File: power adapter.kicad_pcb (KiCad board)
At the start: 2 copper layers, 63.5 x 38.1 mm, 12 parts

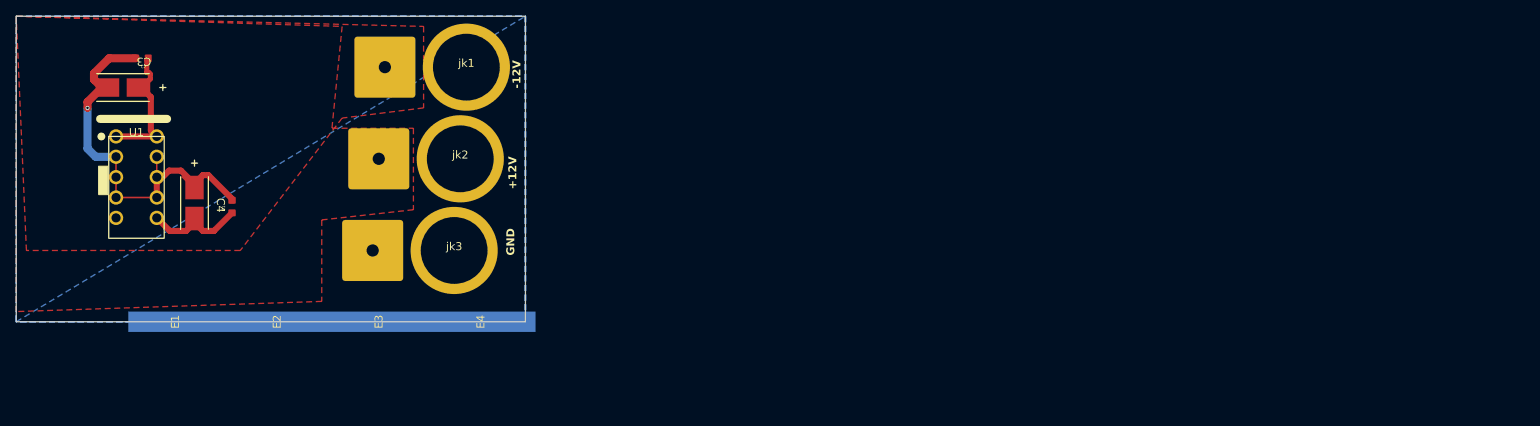
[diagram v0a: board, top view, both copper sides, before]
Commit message: added new board outline
used an .svg file from corel to define board outlinr and resized the banana jack holes and scale for the model
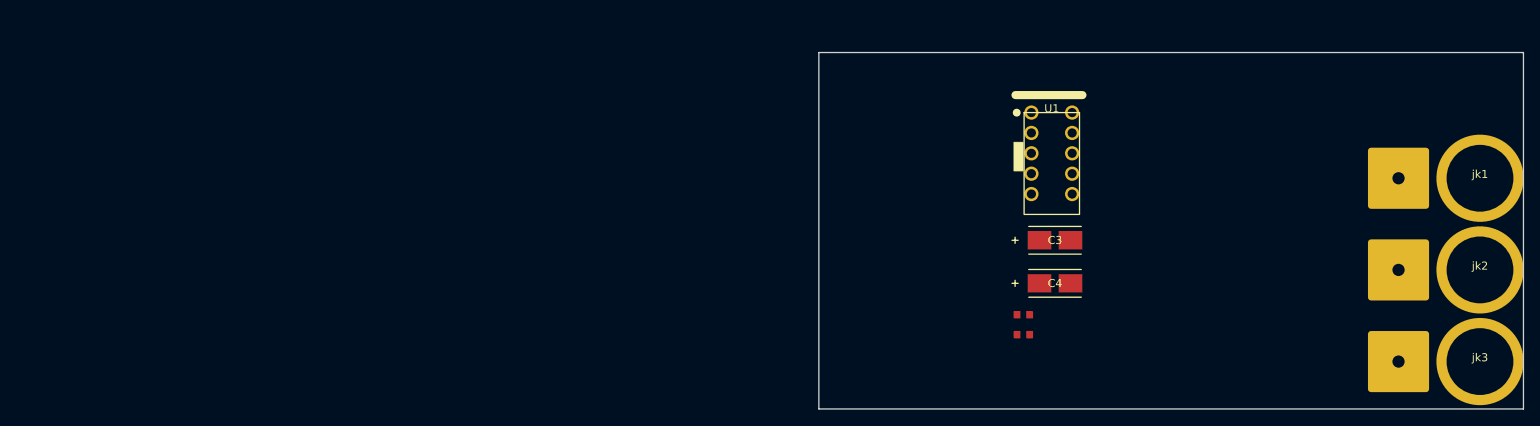
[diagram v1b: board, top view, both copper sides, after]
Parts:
- removed E1, E2, E3, E4: ~, adpterpcblib:edge
- moved jk3 128.7 mm to (207.9, 119.3)
- moved jk2 127.9 mm to (207.9, 107.8)
- moved jk1 127.2 mm to (207.9, 96.4)
- moved C3 117.8 mm to (154.9, 104.1), turned to 0 degrees
- moved C2 115.2 mm to (151.0, 115.9), turned to 0 degrees
- moved U1 114.2 mm to (154.5, 88.2)
- moved C4 107.8 mm to (154.9, 109.5), turned to 0 degrees
- moved C1 99.6 mm to (151.0, 113.4), turned to 0 degrees
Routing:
- net GND: track 55.3 -> 0.00 mm, vias 1 -> 0
- net +12V: track 17.0 -> 0.00 mm
- net -12V: track 12.4 -> 0.00 mm
- removed copper zone on B.Cu, net (none)
- removed copper zone on B.Cu, net +12V
- removed copper zone on F.Cu, net +12V
- removed copper zone on F.Cu, net -12V
- removed copper zone on B.Cu, net GND
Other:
- board size 63.5 x 38.1 mm -> 87.9 x 44.5 mm
- board text removed: "+12V"
- board text removed: "-12V"
- board text removed: "GND"

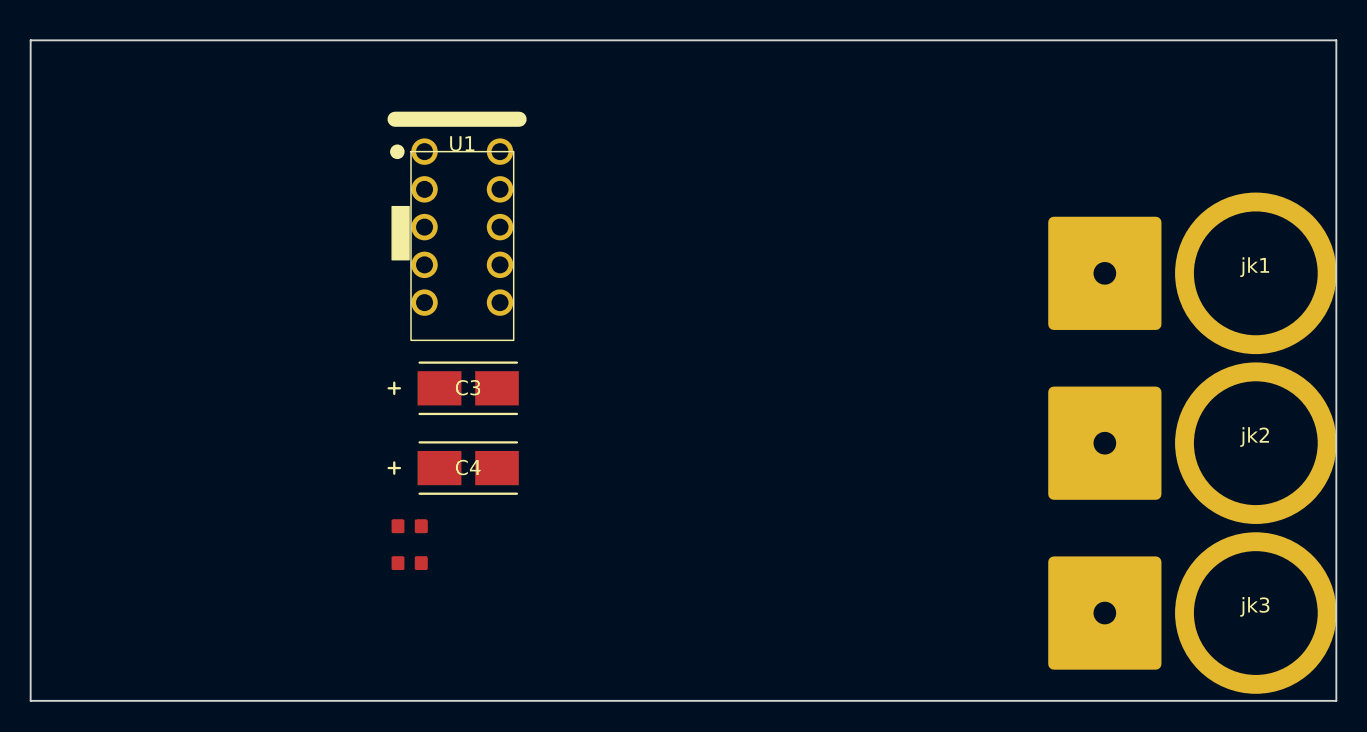
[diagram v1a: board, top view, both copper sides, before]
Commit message: added dimensions
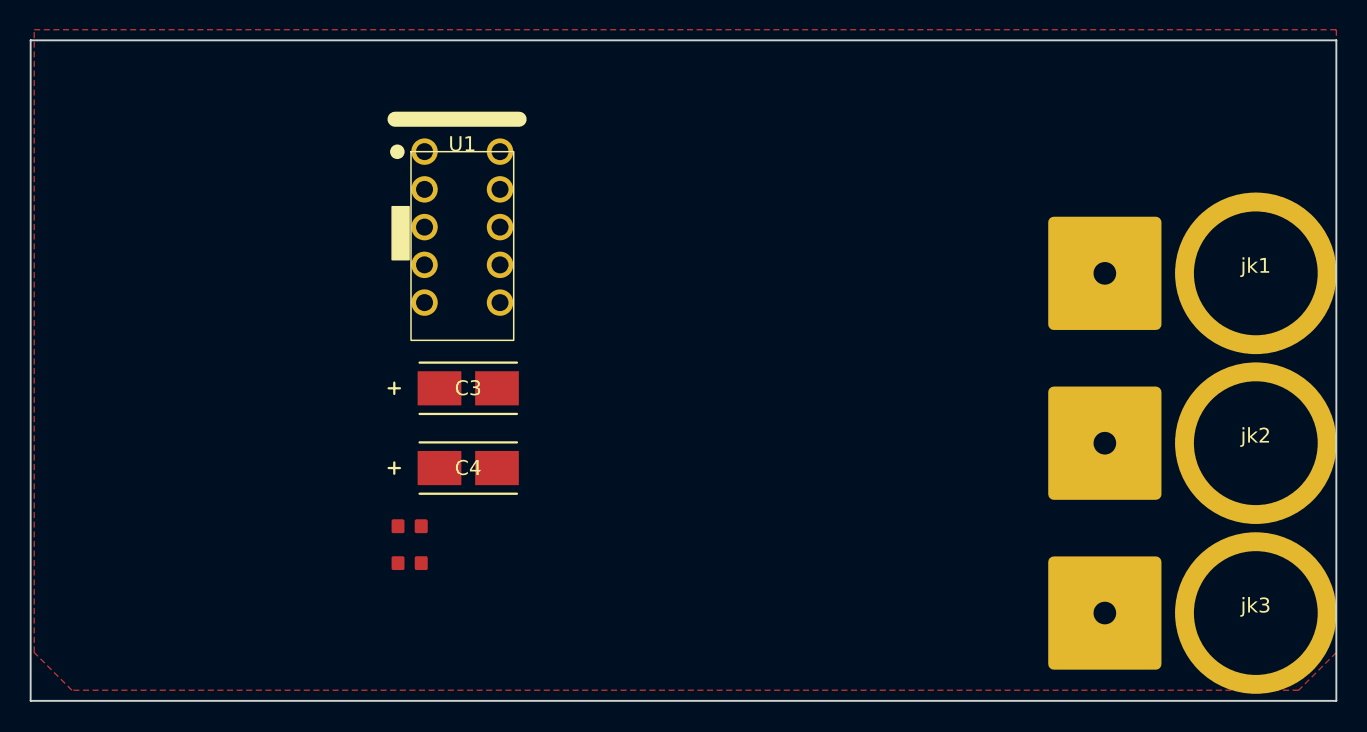
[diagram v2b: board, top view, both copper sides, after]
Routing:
- added copper zone on F.Cu, net GND
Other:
- board text added: "+12V"
- board text added: "-12V"
- board text added: "GND"
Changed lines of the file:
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@@
 		(layer "Edge.Cuts")
+	)
+	(gr_text "-12V"
+		(at 186.85 98.38 0)
+		(layer "F.Mask" knockout)
+		(effects
+			(font
+				(size 1 1)
+				(thickness 0.2)
+				(bold yes)
+			)
+			(justify left bottom)
+		)
+	)
+	(gr_text "GND"
+		(at 187.29 119 0)
+		(layer "F.Mask" knockout)
+		(effects
+			(font
+				(size 1 1)
+				(thickness 0.2)
+				(bold yes)
+			)
+			(justify left bottom)
+		)
+	)
+	(gr_text "+12V"
+		(at 185.36 109.38 0)
+		(layer "F.Mask" knockout)
+		(effects
+			(font
+				(size 1 1)
+				(thickness 0.2)
+				(bold yes)
+			)
+			(justify left bottom)
+		)
+	)
+	(dimension
+		(type aligned)
+		(layer "User.1")
+		(pts
+			(xy 125.491731 80.724935) (xy 213.48 80.724935)
+		)
+		(height -11.154935)
+		(gr_text "3464.1051 mils"
+			(at 169.485866 68.42 0)
+			(layer "User.1")
+			(effects
+				(font
+					(size 1 1)
+					(thickness 0.15)
+				)
+			)
+		)
+		(format
+			(prefix "")
+			(suffix "")
+			(units 3)
+			(units_format 1)
+			(precision 4)
+		)
+		(style
+			(thickness 0.1)
+			(arrow_length 1.27)
+			(text_position_mode 0)
+			(extension_height 0.58642)
+			(extension_offset 0.5) keep_text_aligned)
+	)
+	(dimension
+		(type aligned)
+		(layer "User.1")
+		(pts
+			(xy 213.358269 80.724935) (xy 213.358269 125.175066)
+		)
+		(height -9.211731)
+		(gr_text "1750.0052 mils"
+			(at 221.42 102.950001 90)
+			(layer "User.1")
+			(effects
+				(font
+					(size 1 1)
+					(thickness 0.15)
+				)
+			)
+		)
+		(format
+			(prefix "")
+			(suffix "")
+			(units 3)
+			(units_format 1)
+			(precision 4)
+		)
+		(style
+			(thickness 0.1)
+			(arrow_length 1.27)
+			(text_position_mode 0)
+			(extension_height 0.58642)
+			(extension_offset 0.5) keep_text_aligned)
+	)
+	(zone
+		(net 2)
+		(net_name "GND")
+		(layer "F.Cu")
+		(hatch edge 0.5)
+		(connect_pads
+			(clearance 0.5)
+		)
+		(min_thickness 0.25)
+		(filled_areas_thickness no)
+		(fill yes
+			(thermal_gap 0.5)
+			(thermal_bridge_width 0.5)
+		)
+		(polygon
+			(pts
+				(xy 125.73 80.01) (xy 213.36 80.01) (xy 213.36 121.92) (xy 210.82 124.46) (xy 128.27 124.46) (xy 125.73 121.92)
+			)
+		)
 	)
 	(group ""

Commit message: more routing
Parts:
- moved C2 32.6 mm to (166.7, 87.3), turned to -90 degrees
- moved C3 16.3 mm to (161.3, 89.2), turned to -90 degrees
- moved C4 7.12 mm to (154.5, 102.4)
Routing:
- net -12V: track 0.00 -> 164.6 mm
- net +12V: track 0.00 -> 67.0 mm
- removed copper zone on F.Cu, net GND
